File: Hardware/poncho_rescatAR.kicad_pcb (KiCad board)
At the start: 2 copper layers, 34 parts, among them P1 5V_OUT, P2 CONN_8, SW1 Reset_ciaa, U1 LM317T, U2 LM7805

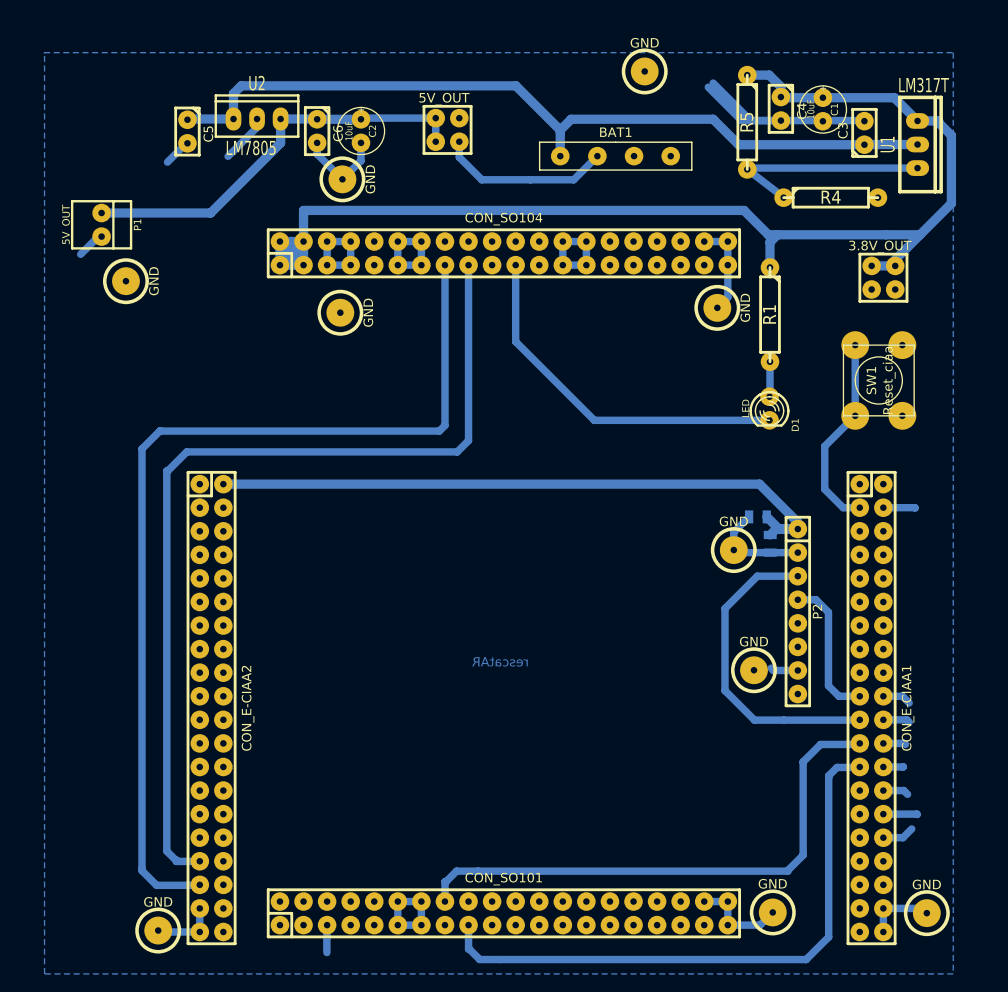
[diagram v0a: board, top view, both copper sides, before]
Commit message: retoques al pcb, cambio por el footprint erroneo del LM317
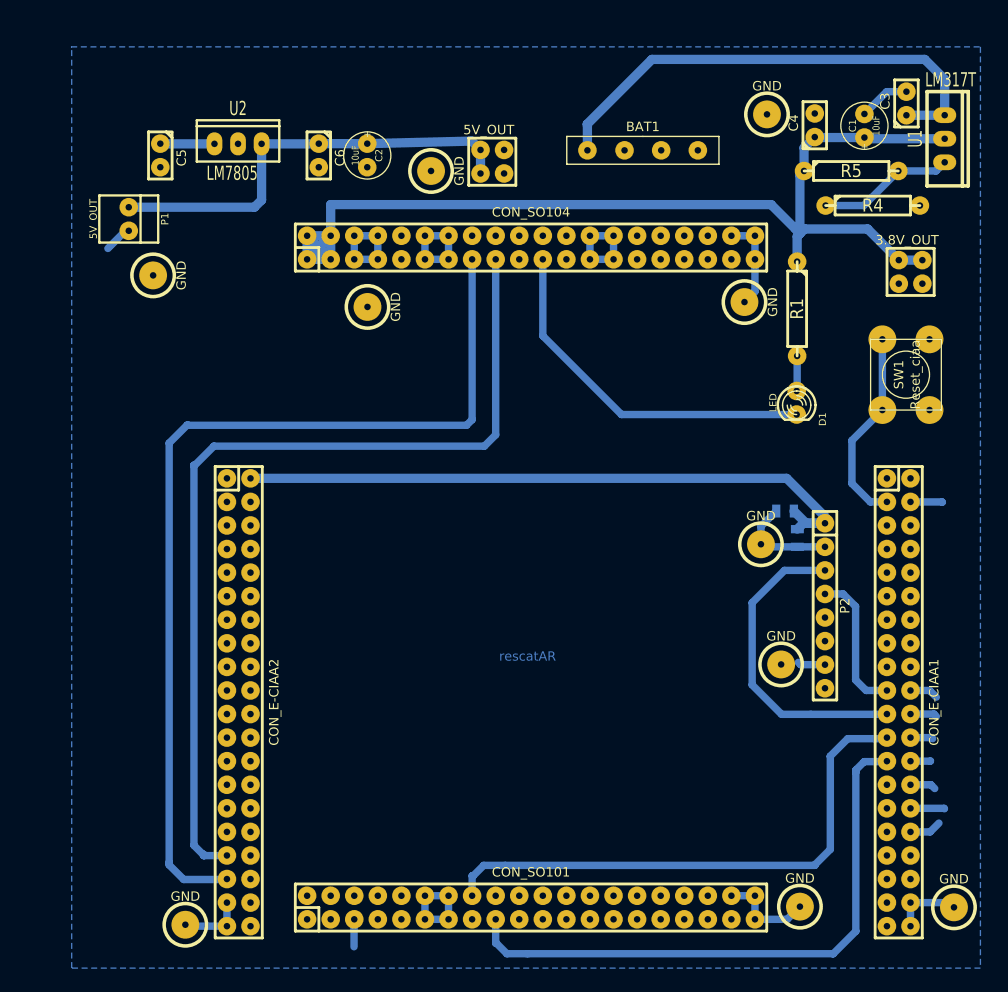
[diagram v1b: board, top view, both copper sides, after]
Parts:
- moved GND 14.0 mm to (243.1, 32.4)
- moved R5 12.4 mm to (252.2, 38.5), turned to 0 degrees
- moved GND 9.59 mm to (206.9, 38.5)
- moved 5V_OUT 5.92 mm to (213.5, 37.5)
- moved C3 5.53 mm to (258.1, 31.2)
- moved C1 4.81 mm to (253.6, 33.6), turned to 90 degrees
- moved R4 4.60 mm to (254.5, 42.2)
- moved C4 4.06 mm to (248.2, 33.5), turned to 90 degrees
- moved C5 3.90 mm to (177.7, 36.8)
- moved U2 3.37 mm to (186.1, 35.5)
- moved 3.8V_OUT 2.99 mm to (258.6, 49.3)
- moved C8 2.99 mm to (245.0, 75.1)
- moved CON_E-CIAA2 2.99 mm to (186.2, 95.7)
- moved CON_SO101 2.99 mm to (217.7, 117.8)
- moved CON_SO104 2.99 mm to (217.7, 46.7)
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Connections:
- U1 pad 2: /VCC_3.8V -> VCC
- U1 pad 3: VCC -> /VCC_3.8V
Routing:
- net /GND: track 184.1 -> 125.5 mm
- net VCC: track 88.2 -> 59.0 mm
- net /VCC_3.8V: track 136.6 -> 115.9 mm
- net N-0000010: track 23.4 -> 14.8 mm
- net N-000001: track 44.3 -> 47.2 mm

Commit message: retoques para prueba final
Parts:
- moved CON_SO101 2.65 mm to (215.0, 117.8)
- moved CON_SO104 2.65 mm to (215.0, 46.7)
- moved 5V_OUT 0.39 mm to (213.7, 37.8)
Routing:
- net VCC: track 59.0 -> 105.4 mm
- net /GND: track 125.5 -> 165.9 mm
- net /GE864_ON_OFF: track 103.4 -> 99.0 mm
- net /GE864_RESET: track 98.4 -> 94.2 mm
- net /VCC_3.8V: track 115.9 -> 112.5 mm
- net /RS232_RXD: track 58.9 -> 61.5 mm
- net /STATUS_LED: track 39.1 -> 41.4 mm

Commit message: rotoques pcb
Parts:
- C7: footprint SM0805 -> C1; moved to F.Cu
- C8: footprint SM0805 -> C1V5; moved to F.Cu
- moved C8 5.91 mm to (248.8, 70.6), turned to 90 degrees
- moved C7 2.43 mm to (245.3, 75.8)
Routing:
- net /GND: track 165.9 -> 175.5 mm
- net /VCC_5V: track 71.5 -> 72.1 mm
- added copper zone on F.Cu, net /GND
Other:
- board text added: "12V"
- board text added: "3.8V"
- board text added: "5V"
- board text added: "rescatAR - T. de Proyecto 1 2015 Viatge Bastien Minig Traverso Marcelo Barbusse Nicolas Vázquez Facundo Garcia Manuel"

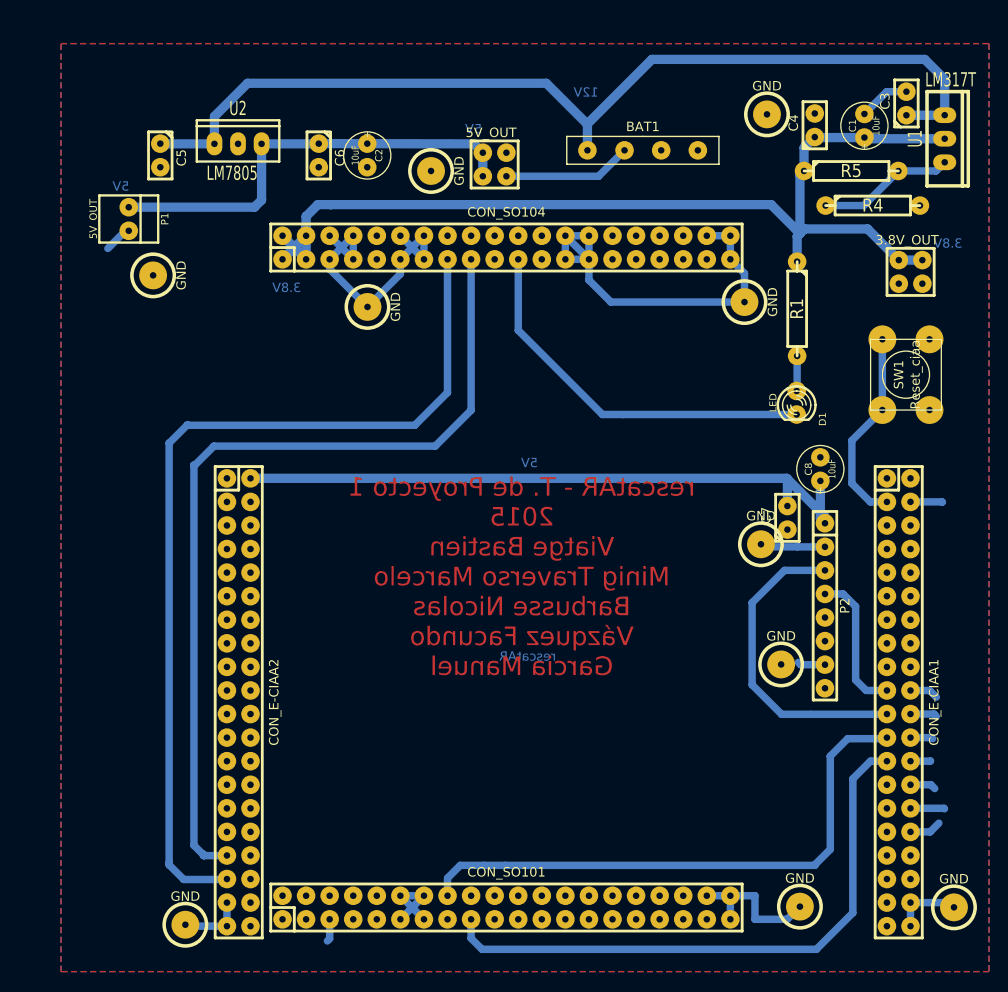
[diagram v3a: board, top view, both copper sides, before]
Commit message: Correccion error en PCB y creacion de pdf para tranferir al cobre
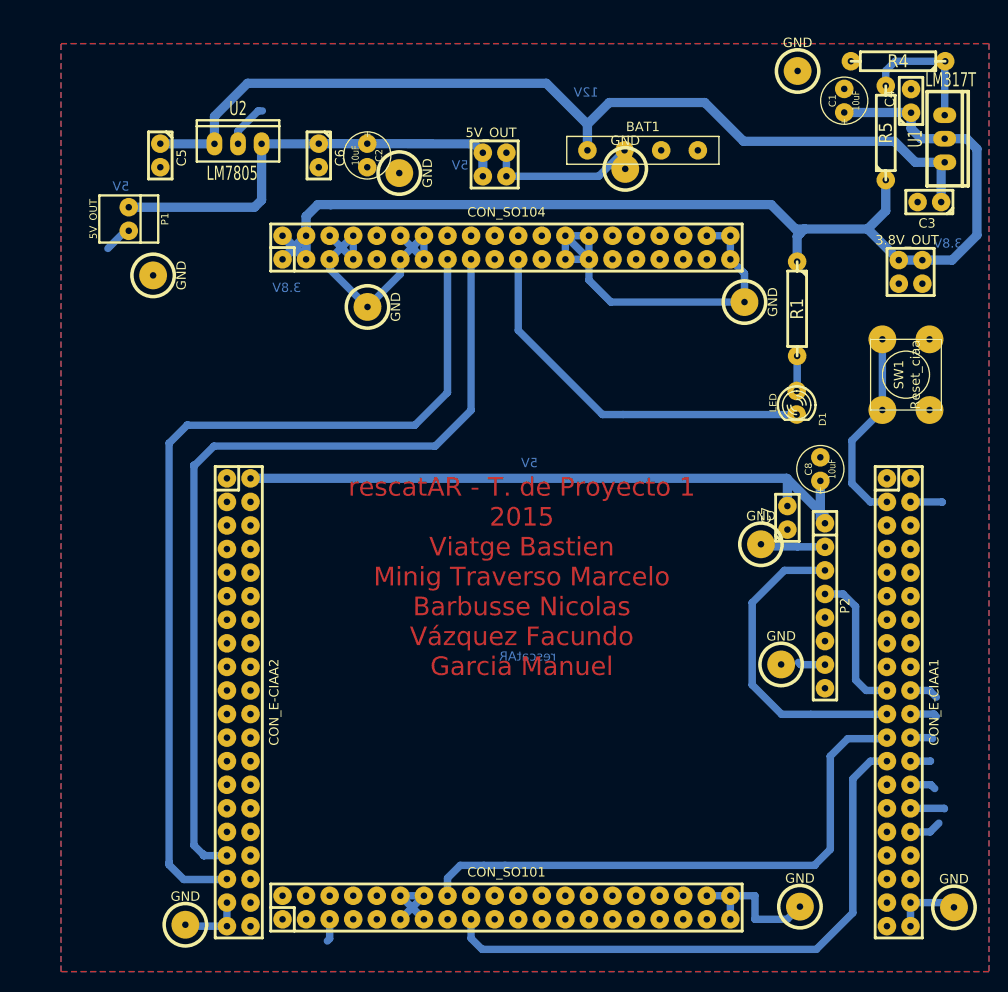
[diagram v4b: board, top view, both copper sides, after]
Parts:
- added GND: P***, 1pin, F.Cu at (227.8, 38.2)
- moved R4 15.8 mm to (257.2, 26.6), turned to 180 degrees
- moved C3 10.9 mm to (260.6, 41.8), turned to 180 degrees
- moved C4 10.7 mm to (258.6, 30.9)
- moved GND 5.72 mm to (246.4, 27.7)
- moved R5 5.54 mm to (255.9, 34.4), turned to 90 degrees
- moved C1 3.47 mm to (251.4, 30.9)
- moved GND 3.43 mm to (203.4, 38.7)
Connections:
- U1 pad 1: N-0000010 -> VCC
- U1 pad 2: VCC -> N-0000010
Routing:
- net /VCC_3.8V: track 112.5 -> 126.6 mm
- net VCC: track 105.4 -> 101.7 mm
- net /GND: track 175.5 -> 177.5 mm

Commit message: retoques al PCB, agregado de disipadores
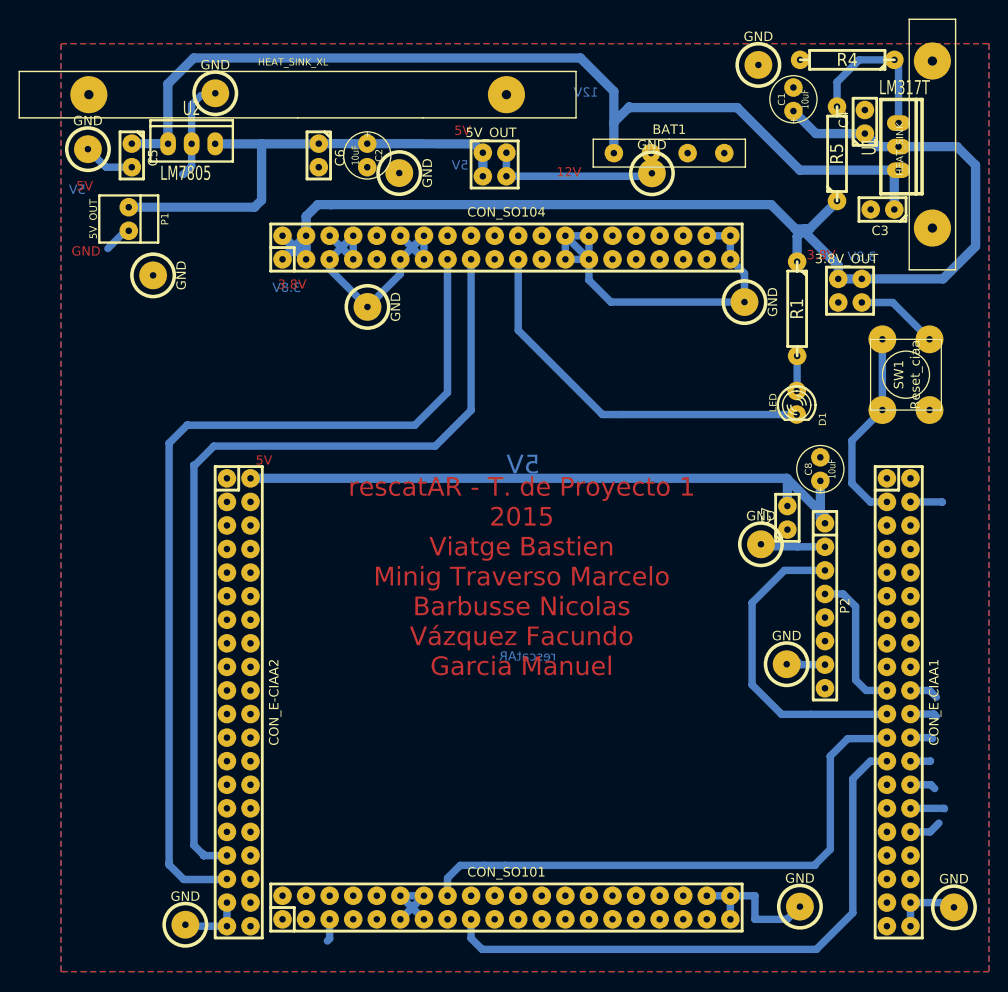
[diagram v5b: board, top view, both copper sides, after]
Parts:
- added GND: P***, 1pin, F.Cu at (183.6, 30.1)
- added GND: P***, 1pin, F.Cu at (169.9, 36.1)
- added HEAT_SINK: Val**, heat_sink_LM3717, F.Cu at (260.9, 35.6)
- added HEAT_SINK_XL: Val**, heat_sink_LM3717_XL, F.Cu at (192.5, 30.2)
- moved 3.8V_OUT 6.83 mm to (252.0, 51.4)
- moved R5 5.71 mm to (250.6, 36.6)
- moved C1 5.48 mm to (245.9, 30.7)
- moved R4 5.48 mm to (251.7, 26.5)
- moved C4 5.46 mm to (253.6, 33.1)
- moved C3 5.11 mm to (255.5, 42.6)
- moved U1 5.05 mm to (257.2, 35.8)
- moved U2 5.00 mm to (181.1, 35.5)
- moved GND 4.27 mm to (242.2, 27.0)
- moved C5 3.07 mm to (174.6, 36.8)
- moved GND 2.91 mm to (230.7, 38.7)
- moved BAT1 2.87 mm to (232.6, 36.5)
- moved GND 0.60 mm to (245.2, 91.6)
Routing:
- net /GND: track 177.5 -> 200.5 mm
- net /VCC_3.8V: track 126.6 -> 132.7 mm
- net N-000001: track 47.5 -> 52.5 mm
- net VCC: track 101.7 -> 106.4 mm
- net N-0000010: track 14.3 -> 16.8 mm
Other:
- board text added: "GND"

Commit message: Modificaciones finales al pcb
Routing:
- net /GE864_RESET: track 94.2 -> 0.00 mm
- net /GND: track 200.5 -> 228.7 mm
